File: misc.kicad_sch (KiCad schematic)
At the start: 55 parts, among them J10 Molex_KK_1x4_0470531000, J11 Molex_KK_1x4_0470531000, J9 Molex_KK_1x4_0470531000, Q10 MMBT3904LT1G, Q5 BSS138-7-F, Q6 BSS84AKW, Q7 BSS138-7-F, Q8 BSS138-7-F, Q9 MMBT3904LT1G, U24 ADT7476AARQZ, U25 74LVC1G157-Q100H_SOT457, U26 74LVC1G157-Q100H_SOT457, U27 NTS0102_TSSOP, U28 NTS0102_TSSOP, U29 NTS0102_TSSOP

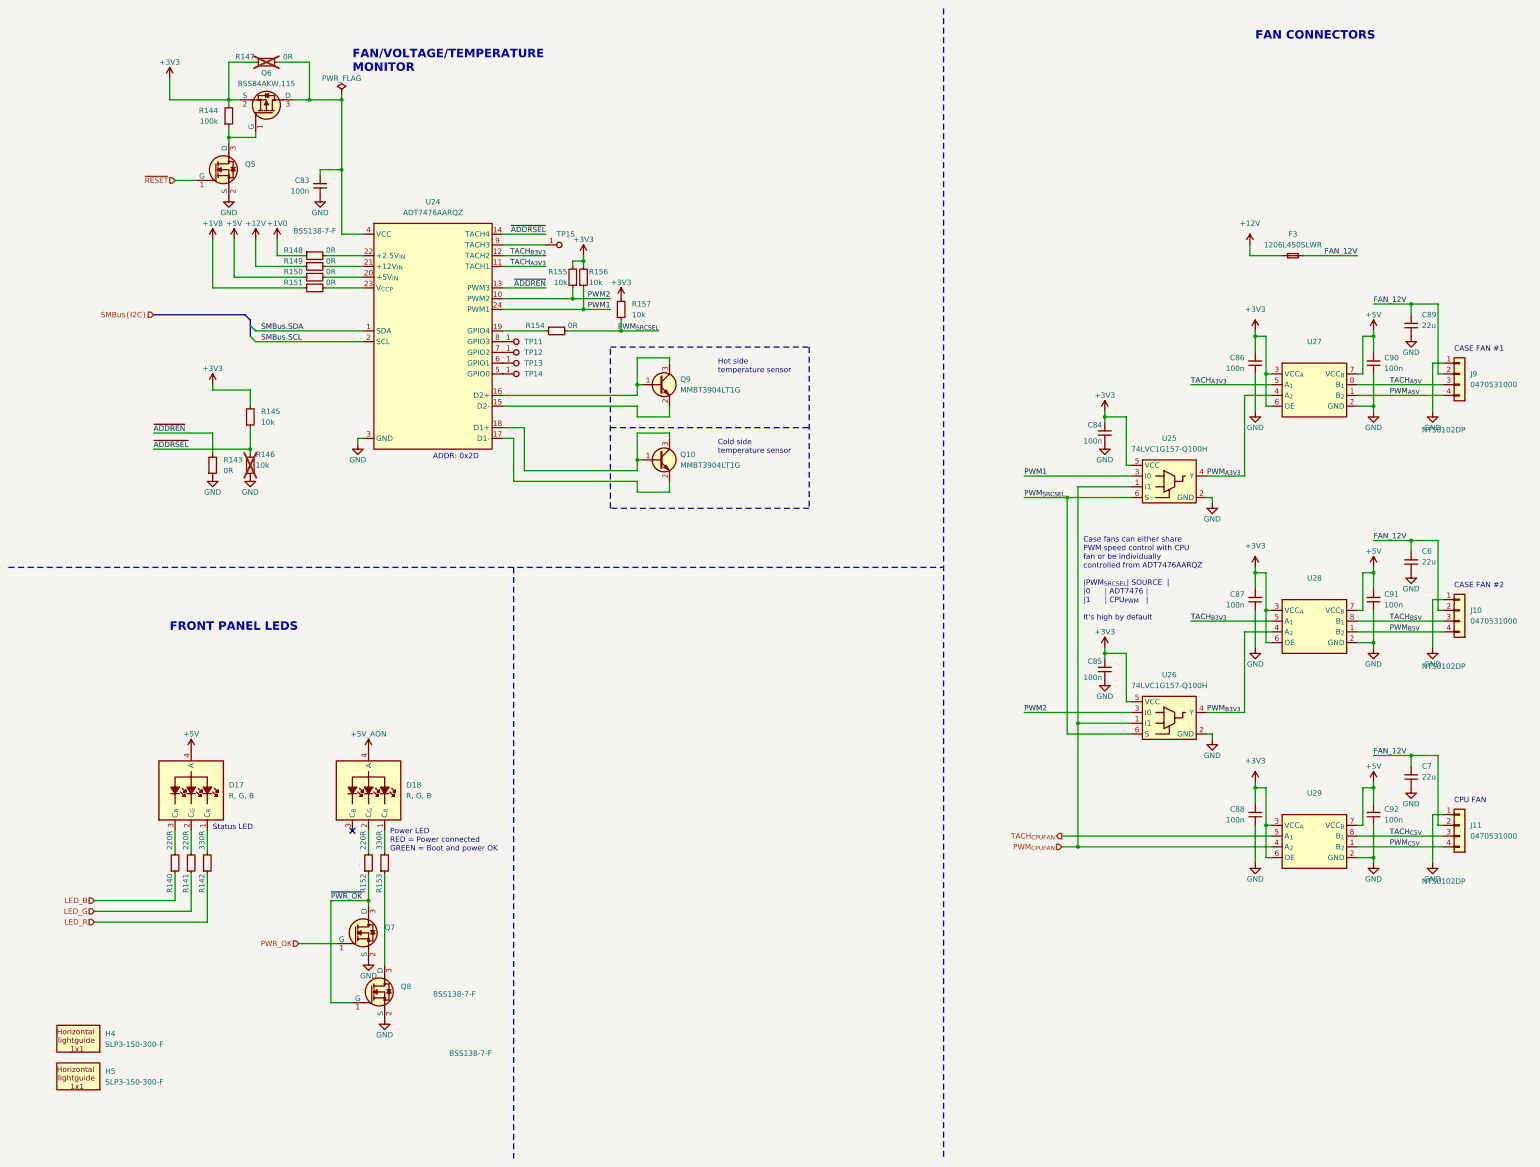
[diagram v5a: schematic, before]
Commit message: [#65447] Fix rotated LEDs, overlapping text and symbols, add rules
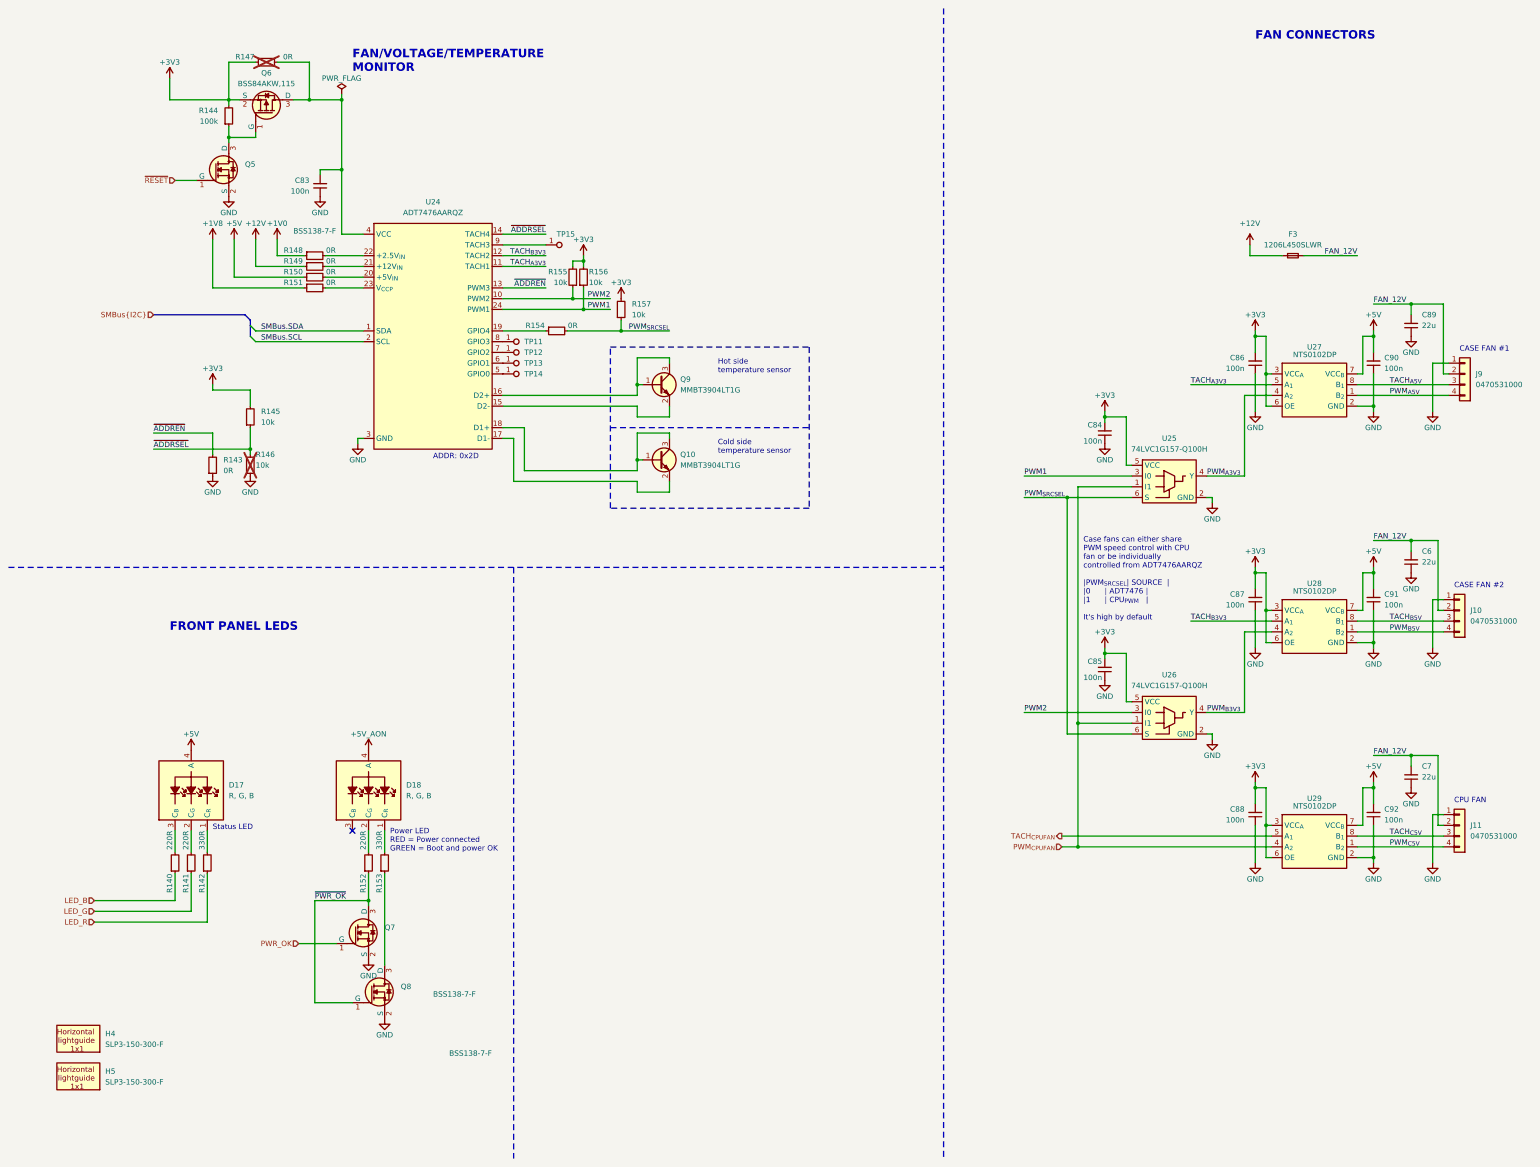
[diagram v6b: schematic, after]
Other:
- moved on the sheet: J9
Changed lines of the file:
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@@
     (stroke (width 0) (type default))
   )
-  (wire (pts (xy 344.17 82.55) (xy 350.52 82.55))
+  (wire (pts (xy 344.17 82.55) (xy 351.79 82.55))
     (stroke (width 0) (type default))
   )
@@
     (stroke (width 0) (type default))
   )
-  (wire (pts (xy 97.79 223.52) (xy 88.9 223.52))
-    (stroke (width 0) (type default))
-  )
   (wire (pts (xy 271.78 163.83) (xy 271.78 165.1))
     (stroke (width 0) (type default))
@@
     (stroke (width 0) (type default))
   )
-  (wire (pts (xy 350.52 99.06) (xy 350.52 82.55))
+  (wire (pts (xy 351.79 99.06) (xy 351.79 82.55))
     (stroke (width 0) (type default))
   )
@@
     (stroke (width 0) (type default))
   )
-  (wire (pts (xy 331.47 101.6) (xy 351.79 101.6))
+  (wire (pts (xy 331.47 101.6) (xy 353.06 101.6))
     (stroke (width 0) (type default))
   )
@@
     (stroke (width 0) (type default))
   )
-  (wire (pts (xy 88.9 223.52) (xy 88.9 247.65))
+  (wire (pts (xy 85.09 223.52) (xy 85.09 247.65))
     (stroke (width 0) (type default))
   )
@@
     (stroke (width 0) (type default))
   )
-  (wire (pts (xy 351.79 99.06) (xy 350.52 99.06))
+  (wire (pts (xy 353.06 99.06) (xy 351.79 99.06))
     (stroke (width 0) (type default))
   )
@@
     (stroke (width 0) (type default))
   )
-  (wire (pts (xy 166.37 88.9) (xy 157.48 88.9))
+  (wire (pts (xy 168.91 88.9) (xy 157.48 88.9))
     (stroke (width 0) (type default))
   )
@@
     (stroke (width 0) (type default))
   )
+  (wire (pts (xy 85.09 223.52) (xy 97.79 223.52))
+    (stroke (width 0) (type default))
+  )
   (wire (pts (xy 309.88 90.17) (xy 307.34 90.17))
     (stroke (width 0) (type default))
@@
     (stroke (width 0) (type default))
   )
-  (wire (pts (xy 88.9 247.65) (xy 93.98 247.65))
+  (wire (pts (xy 85.09 247.65) (xy 93.98 247.65))
     (stroke (width 0) (type default))
   )
@@
     (stroke (width 0) (type default))
   )
-  (wire (pts (xy 331.47 104.14) (xy 351.79 104.14))
+  (wire (pts (xy 331.47 104.14) (xy 353.06 104.14))
     (stroke (width 0) (type default))
   )
@@
     (stroke (width 0) (type default))
   )
-  (wire (pts (xy 351.79 96.52) (xy 349.25 96.52))
+  (wire (pts (xy 353.06 96.52) (xy 349.25 96.52))
     (stroke (width 0) (type default))
   )
@@
     (effects (font (size 1.27 1.27)) (justify left bottom))
   )
-  (text "CASE FAN #1" (at 354.33 93.98 0)
+  (text "CASE FAN #1" (at 355.6 93.98 0)
     (effects (font (size 1.27 1.27)) (justify left bottom))
   )
@@
     (effects (font (size 1.27 1.27)) (justify left bottom))
   )
-  (label "~{PWR_OK}" (at 88.9 223.52 0) (fields_autoplaced)
+  (label "~{PWR_OK}" (at 85.09 223.52 0) (fields_autoplaced)
     (effects (font (size 1.27 1.27)) (justify left bottom))
   )
@@
     (effects (font (size 1.27 1.27)) (justify right bottom))
   )
-  (label "PWM_{SRCSEL}" (at 166.37 88.9 180) (fields_autoplaced)
+  (label "PWM_{SRCSEL}" (at 168.91 88.9 180) (fields_autoplaced)
     (effects (font (size 1.27 1.27)) (justify right bottom))
   )
@@
   )
   (symbol (lib_id "antmicropower:+3V3") (at 307.34 195.58 0) (unit 1)
-    (in_bom yes) (on_board yes) (dnp no) (fields_autoplaced)
+    (in_bom yes) (on_board yes) (dnp no)
     (property "Reference" "#PWR0211" (at 322.58 195.58 0)
       (effects (font (size 1.27 1.27) (thickness 0.15)) (justify left bottom) hide)
     )
-    (property "Value" "+3V3" (at 307.34 190.5 0)
+    (property "Value" "+3V3" (at 307.34 191.77 0)
       (effects (font (size 1.27 1.27) (thickness 0.15)))
     )
@@
   )
   (symbol (lib_id "antmicroLogicTranslatorsLevelShifters:NTS0102_TSSOP") (at 311.15 99.06 0) (unit 1)
-    (in_bom yes) (on_board yes) (dnp no) (fields_autoplaced)
-    (property "Reference" "U27" (at 321.31 91.44 0)
+    (in_bom yes) (on_board yes) (dnp no)
+    (property "Reference" "U27" (at 321.31 92.71 0)
       (effects (font (size 1.27 1.27) (thickness 0.15)))
     )
@@
       (effects (font (size 1.27 1.27) (thickness 0.15)) (justify left bottom) hide)
     )
-    (property "MPN" "NTS0102DP" (at 346.71 113.03 0)
+    (property "MPN" "NTS0102DP" (at 316.23 95.25 0)
       (effects (font (size 1.27 1.27) (thickness 0.15)) (justify left bottom))
     )
@@
   )
   (symbol (lib_id "antmicropower:+3V3") (at 307.34 88.9 0) (unit 1)
-    (in_bom yes) (on_board yes) (dnp no) (fields_autoplaced)
+    (in_bom yes) (on_board yes) (dnp no)
     (property "Reference" "#PWR0207" (at 322.58 88.9 0)
       (effects (font (size 1.27 1.27) (thickness 0.15)) (justify left bottom) hide)
     )
-    (property "Value" "+3V3" (at 307.34 83.82 0)
+    (property "Value" "+3V3" (at 307.34 85.09 0)
       (effects (font (size 1.27 1.27) (thickness 0.15)))
     )
@@
     )
   )
-  (symbol (lib_id "antmicroWire2BoardConnectors:Molex_KK_1x4_0470531000") (at 351.79 96.52 0) (unit 1)
+  (symbol (lib_id "antmicroWire2BoardConnectors:Molex_KK_1x4_0470531000") (at 353.06 96.52 0) (unit 1)
     (in_bom yes) (on_board yes) (dnp no)
-    (property "Reference" "J9" (at 358.14 99.06 0)
+    (property "Reference" "J9" (at 359.41 99.06 0)
       (effects (font (size 1.27 1.27) (thickness 0.15)) (justify left))
     )
-    (property "Value" "Molex_KK_1x4_0470531000" (at 372.11 106.68 0)
+    (property "Value" "Molex_KK_1x4_0470531000" (at 373.38 106.68 0)
       (effects (font (size 1.27 1.27) (thickness 0.15)) (justify left bottom) hide)
     )
-    (property "Footprint" "antmicro-footprints:Conn_Molex_KK_1x4_0470531000" (at 372.11 109.22 0)
+    (property "Footprint" "antmicro-footprints:Conn_Molex_KK_1x4_0470531000" (at 373.38 109.22 0)
       (effects (font (size 1.27 1.27) (thickness 0.15)) (justify left bottom) hide)
     )
-    (property "Datasheet" "https://tools.molex.com/pdm_docs/sd/470531000_sd.pdf" (at 372.11 111.76 0)
+    (property "Datasheet" "https://tools.molex.com/pdm_docs/sd/470531000_sd.pdf" (at 373.38 111.76 0)
       (effects (font (size 1.27 1.27) (thickness 0.15)) (justify left bottom) hide)
     )
-    (property "MPN" "0470531000" (at 358.14 101.6 0)
+    (property "MPN" "0470531000" (at 359.41 101.6 0)
       (effects (font (size 1.27 1.27) (thickness 0.15)) (justify left))
     )
-    (property "Manufacturer" "Molex" (at 372.11 114.3 0)
+    (property "Manufacturer" "Molex" (at 373.38 114.3 0)
       (effects (font (size 1.27 1.27) (thickness 0.15)) (justify left bottom) hide)
     )
-    (property "Author" "Antmicro" (at 372.11 116.84 0)
+    (property "Author" "Antmicro" (at 373.38 116.84 0)
       (effects (font (size 1.27 1.27) (thickness 0.15)) (justify left bottom) hide)
     )
-    (property "License" "Apache-2.0" (at 372.11 119.38 0)
+    (property "License" "Apache-2.0" (at 373.38 119.38 0)
       (effects (font (size 1.27 1.27) (thickness 0.15)) (justify left bottom) hide)
     )
@@
   )
   (symbol (lib_id "antmicroLogicTranslatorsLevelShifters:NTS0102_TSSOP") (at 311.15 154.94 0) (unit 1)
-    (in_bom yes) (on_board yes) (dnp no) (fields_autoplaced)
-    (property "Reference" "U28" (at 321.31 147.32 0)
+    (in_bom yes) (on_board yes) (dnp no)
+    (property "Reference" "U28" (at 321.31 148.59 0)
       (effects (font (size 1.27 1.27) (thickness 0.15)))
     )
@@
       (effects (font (size 1.27 1.27) (thickness 0.15)) (justify left bottom) hide)
     )
-    (property "MPN" "NTS0102DP" (at 346.71 168.91 0)
+    (property "MPN" "NTS0102DP" (at 316.23 151.13 0)
       (effects (font (size 1.27 1.27) (thickness 0.15)) (justify left bottom))
     )
@@
   )
   (symbol (lib_id "antmicroLogicTranslatorsLevelShifters:NTS0102_TSSOP") (at 311.15 205.74 0) (unit 1)
-    (in_bom yes) (on_board yes) (dnp no) (fields_autoplaced)
-    (property "Reference" "U29" (at 321.31 198.12 0)
+    (in_bom yes) (on_board yes) (dnp no)
+    (property "Reference" "U29" (at 321.31 199.39 0)
       (effects (font (size 1.27 1.27) (thickness 0.15)))
     )
@@
       (effects (font (size 1.27 1.27) (thickness 0.15)) (justify left bottom) hide)
     )
-    (property "MPN" "NTS0102DP" (at 346.71 219.71 0)
+    (property "MPN" "NTS0102DP" (at 316.23 201.93 0)
       (effects (font (size 1.27 1.27) (thickness 0.15)) (justify left bottom))
     )
@@
   )
   (symbol (lib_id "antmicropower:+3V3") (at 307.34 144.78 0) (unit 1)
-    (in_bom yes) (on_board yes) (dnp no) (fields_autoplaced)
+    (in_bom yes) (on_board yes) (dnp no)
     (property "Reference" "#PWR0209" (at 322.58 144.78 0)
       (effects (font (size 1.27 1.27) (thickness 0.15)) (justify left bottom) hide)
     )
-    (property "Value" "+3V3" (at 307.34 139.7 0)
+    (property "Value" "+3V3" (at 307.34 140.97 0)
       (effects (font (size 1.27 1.27) (thickness 0.15)))
     )

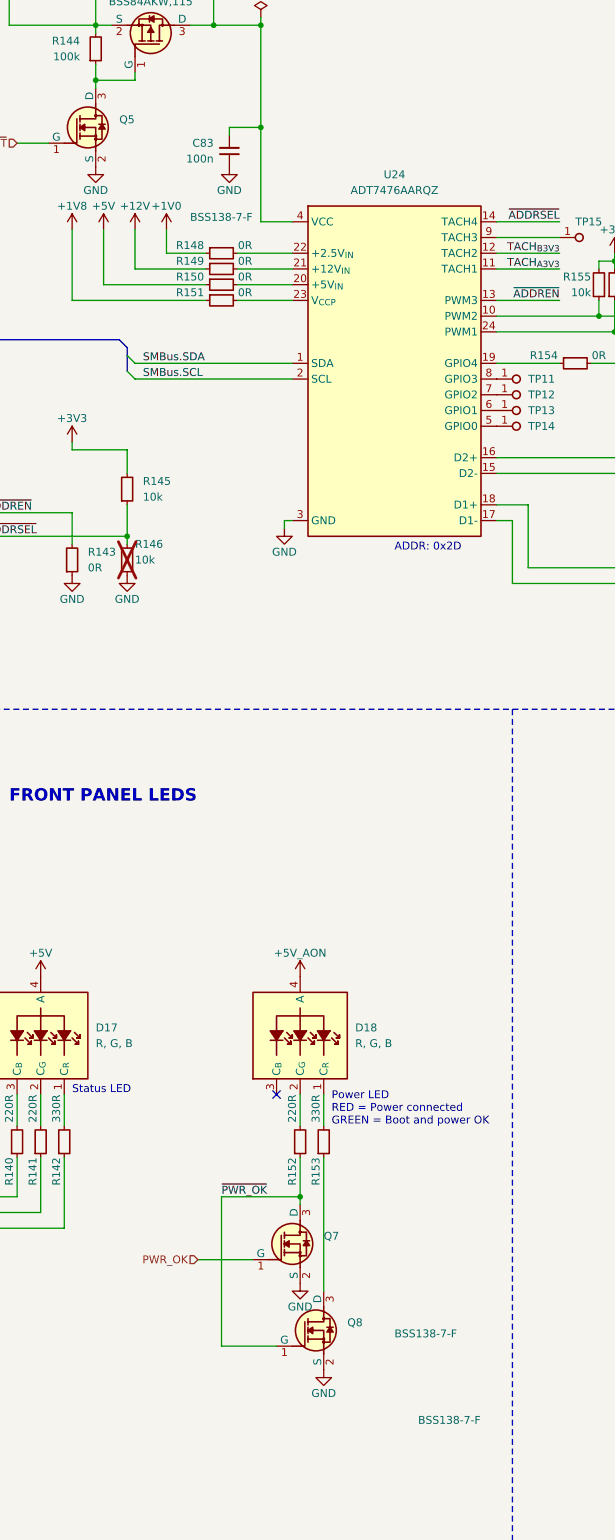
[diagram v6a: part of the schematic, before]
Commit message: [#65447] Layout PCIe, fix net names
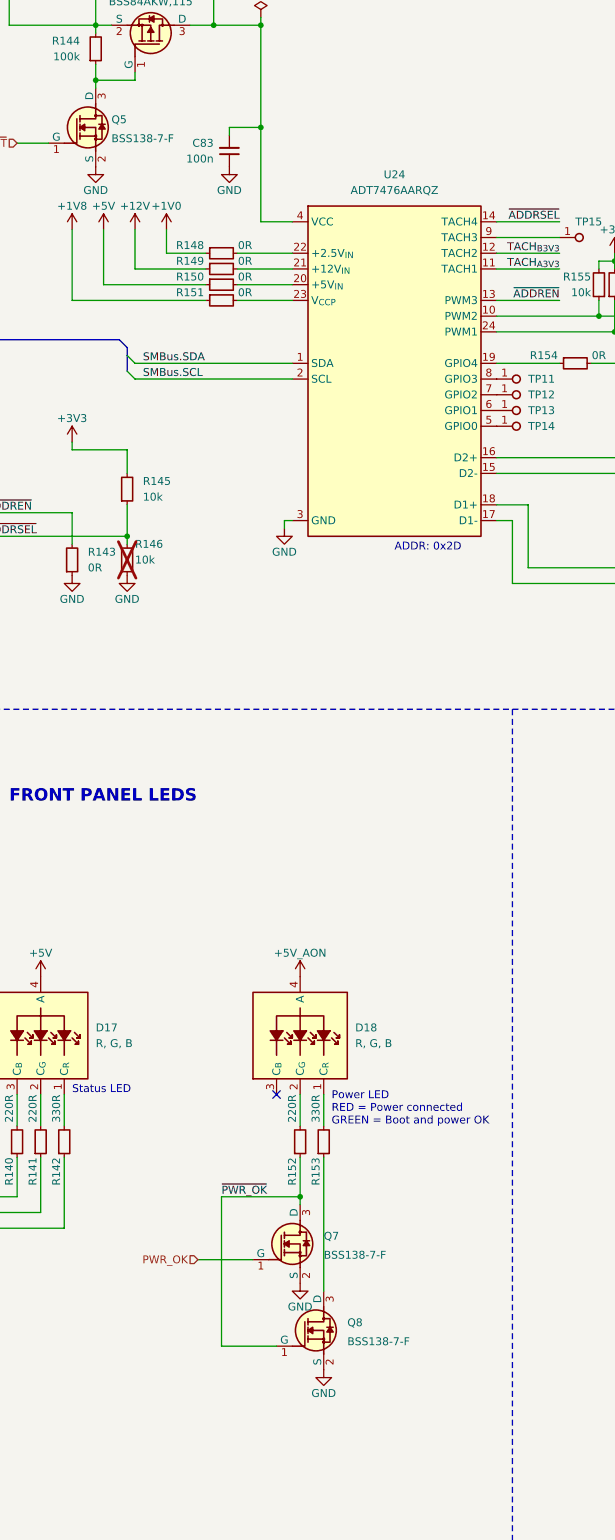
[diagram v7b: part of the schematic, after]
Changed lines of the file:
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@@
   )
   (symbol (lib_id "antmicroTransistorsFETsMOSFETsSingle:BSS138-7-F") (at 90.17 233.68 0) (unit 1)
-    (in_bom yes) (on_board yes) (dnp no) (fields_autoplaced)
+    (in_bom yes) (on_board yes) (dnp no)
     (property "Reference" "Q7" (at 101.6 229.8699 0)
       (effects (font (size 1.27 1.27) (thickness 0.15)) (justify left))
@@
       (effects (font (size 1.27 1.27) (thickness 0.15)) (justify left bottom) hide)
     )
-    (property "MPN" "BSS138-7-F" (at 113.03 246.38 0)
+    (property "MPN" "BSS138-7-F" (at 101.6 233.68 0)
       (effects (font (size 1.27 1.27) (thickness 0.15)) (justify left bottom))
     )
@@
   )
   (symbol (lib_id "antmicroTransistorsFETsMOSFETsSingle:BSS138-7-F") (at 57.15 53.34 0) (unit 1)
-    (in_bom yes) (on_board yes) (dnp no) (fields_autoplaced)
-    (property "Reference" "Q5" (at 68.58 49.53 0)
+    (in_bom yes) (on_board yes) (dnp no)
+    (property "Reference" "Q5" (at 67.31 49.53 0)
       (effects (font (size 1.27 1.27) (thickness 0.15)) (justify left))
     )
@@
       (effects (font (size 1.27 1.27) (thickness 0.15)) (justify left bottom) hide)
     )
-    (property "MPN" "BSS138-7-F" (at 80.01 66.04 0)
+    (property "MPN" "BSS138-7-F" (at 67.31 53.34 0)
       (effects (font (size 1.27 1.27) (thickness 0.15)) (justify left bottom))
     )
@@
   )
   (symbol (lib_id "antmicroTransistorsFETsMOSFETsSingle:BSS138-7-F") (at 93.98 247.65 0) (unit 1)
-    (in_bom yes) (on_board yes) (dnp no) (fields_autoplaced)
+    (in_bom yes) (on_board yes) (dnp no)
     (property "Reference" "Q8" (at 105.41 243.8399 0)
       (effects (font (size 1.27 1.27) (thickness 0.15)) (justify left))
@@
       (effects (font (size 1.27 1.27) (thickness 0.15)) (justify left bottom) hide)
     )
-    (property "MPN" "BSS138-7-F" (at 116.84 260.35 0)
+    (property "MPN" "BSS138-7-F" (at 105.41 247.65 0)
       (effects (font (size 1.27 1.27) (thickness 0.15)) (justify left bottom))
     )
